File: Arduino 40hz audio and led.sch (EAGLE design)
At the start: 18 parts

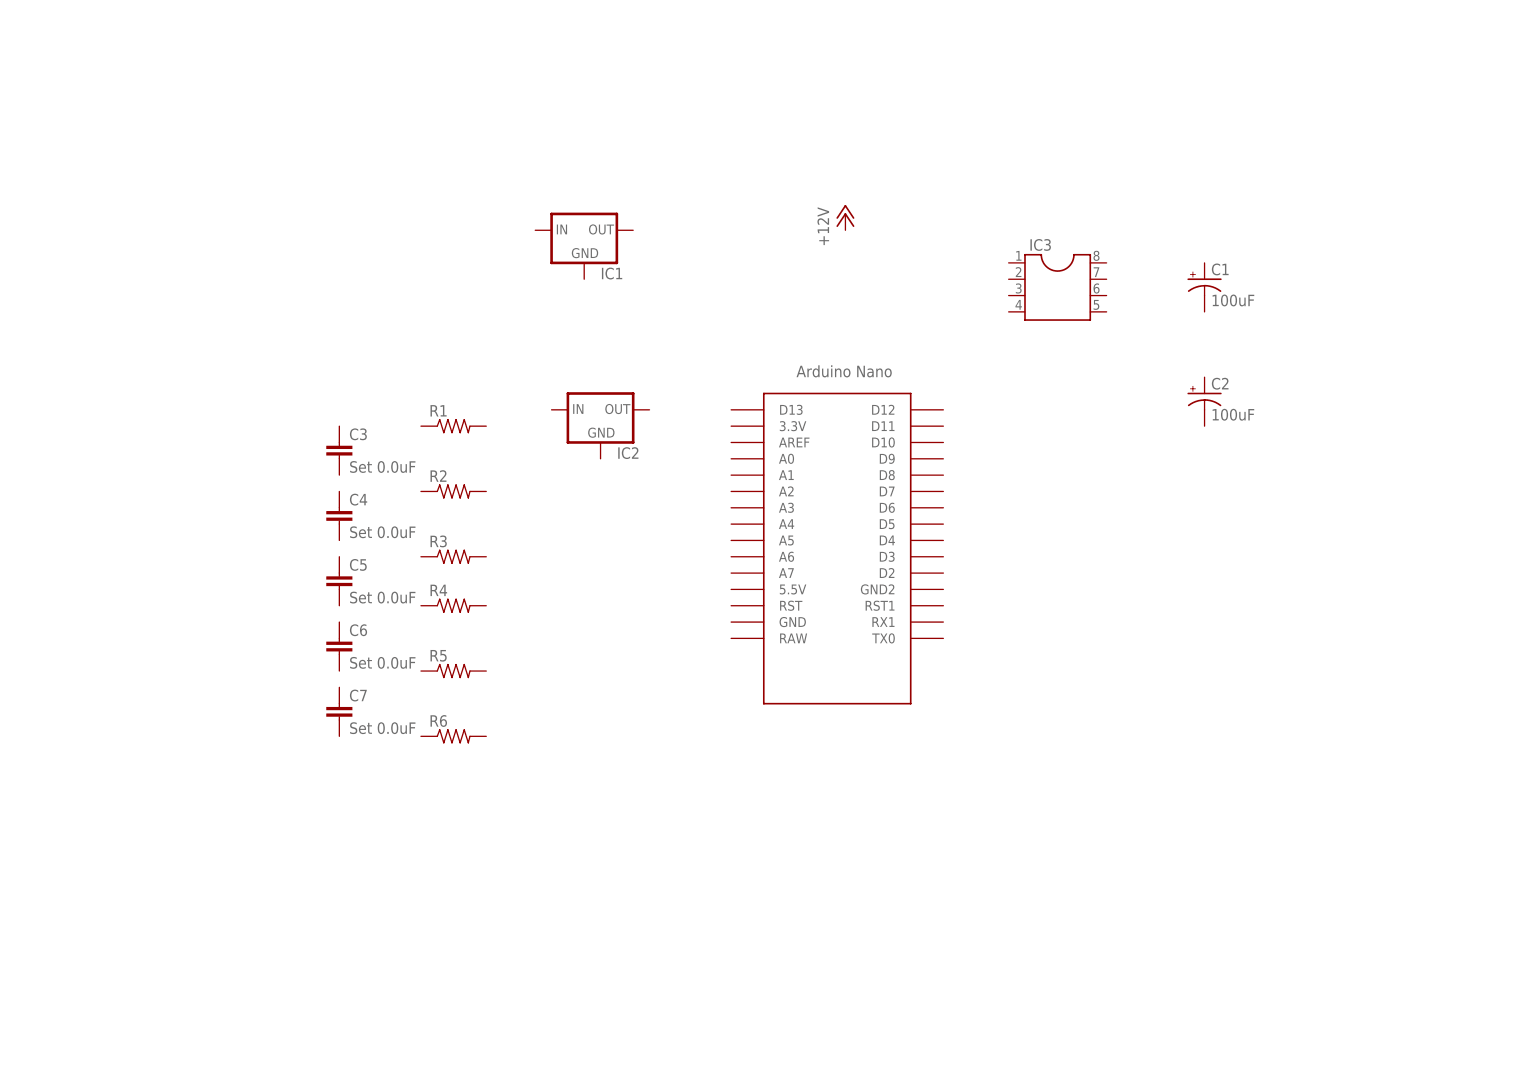
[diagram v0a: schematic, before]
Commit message: Initial schmatic and layout of board
Initial schmatic and layout of board

Still need to move some things around, add a couple of pads and change
some pad sizes.
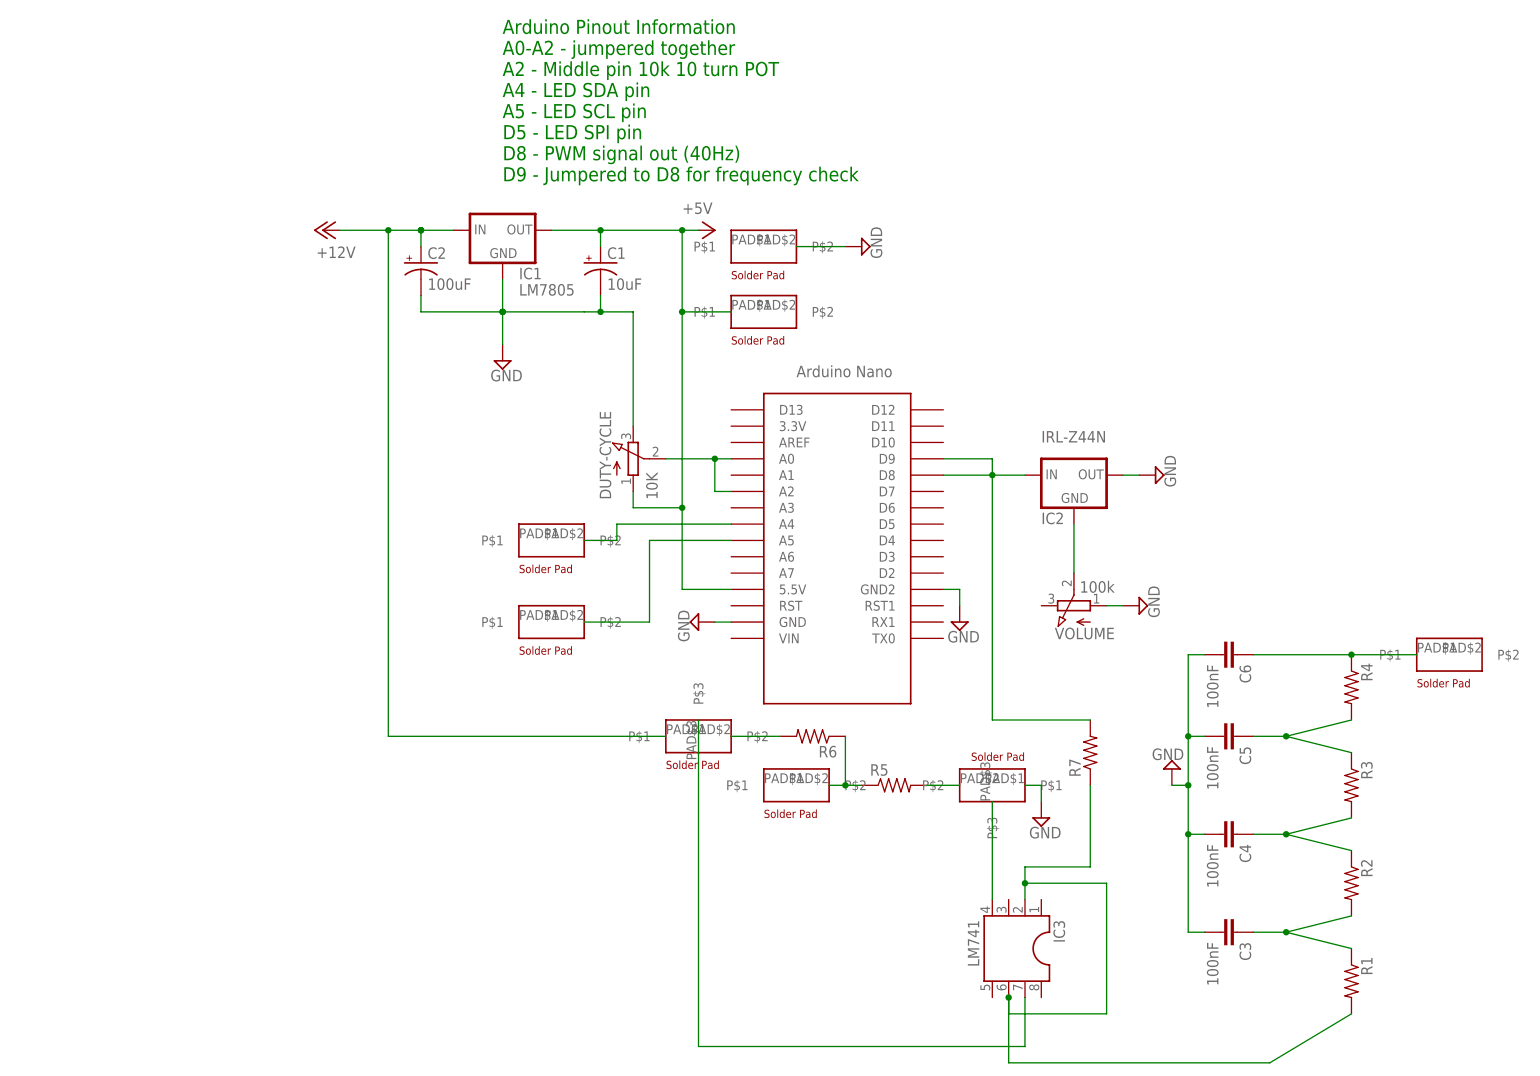
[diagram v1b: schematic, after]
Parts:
- removed C7: Set 0.0uF, jim_muppet_parts:CAP-MEDIUM-MUPPET
- added DUTY-CYCLE: 10K, jim_muppet_parts:POTENTIOMETER
- added LCD-GND: LCD-GND, jim_muppet_parts:PAD-2PIN-RECTANGLE
- added P+2: +5V, jim_muppet_parts:+5V
- added R7: (no value), jim_muppet_parts:RESISTORPTH-1/4W
- added U$2, U$4, U$6, U$7, U$8: PAD-2PIN-RECTANGLE, jim_muppet_parts:PAD-2PIN-RECTANGLE
- added U$3, U$5: PAD-3PIN-RECTANGLE50MIL, jim_muppet_parts:PAD-3PIN-RECTANGLE50MIL
- added VOLUME: 100k, jim_muppet_parts:POTENTIOMETER
- C1: value 100uF -> 10uF
- C3, C4, C5, C6: value Set 0.0uF -> 100nF
- IC1: value (none) -> LM7805
- IC2: value (none) -> IRL-Z44N
- IC3: value (none) -> LM741
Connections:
- new net +12V: C2.+, IC1.IN, P+1.+12V, U$5.P$1
- new net +5V: C1.+, DUTY-CYCLE.A, IC1.OUT, P+2.+5V, U$1.5.5V, U$7.P$1
- new net GND: C1.-, C2.-, C3.2, C4.2, C5.2, C6.2, DUTY-CYCLE.E, IC1.GND, IC2.OUT, LCD-GND.P$2, U$1.GND, U$1.GND2, U$3.P$1, VOLUME.A
- new net N$1: DUTY-CYCLE.S, U$1.A0, U$1.A2
- new net N$10: R5.2, U$3.P$2
- new net N$11: IC3.7, U$5.P$3
- new net N$12: IC3.4, U$3.P$3
- new net N$13: IC3.2, IC3.6, R1.2, R7.1
- new net N$14: U$1.A4, U$4.P$2
- new net N$15: U$1.A5, U$6.P$2
- new net N$2: IC2.IN, R7.2, U$1.D8, U$1.D9
- new net N$3: C3.1, R1.1, R2.2
- new net N$4: C4.1, R2.1, R3.2
- new net N$5: C5.1, R3.1, R4.2
- new net N$6: C6.1, R4.1, U$2.P$1
- new net N$7: R6.2, U$5.P$2
- new net N$8: IC2.GND, VOLUME.S
- new net N$9: R5.1, R6.1, U$8.P$2
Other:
- note added: "Arduino Pinout Information A0-A2 - jumpered together A2 - Middle pin 10k 10 turn POT A4 - LED SDA pin A5 - LED SCL pin D5 - LED SPI pin D8 - PWM signal out (40Hz) D9 - Jumpered to D8 for frequency check"
- moved on the sheet: C1, C2, C3, C4, C5, C6, IC1, IC2, IC3, R1, R2, R3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

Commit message: Updated schematic and board
Updated schematic and board. Made the board more compact.

Still need to fix a few issues with the board
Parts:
- removed LCD-GND: LCD-GND, jim_muppet_parts:PAD-2PIN-RECTANGLE
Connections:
- net GND: no longer LCD-GND.P$2
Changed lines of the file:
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@@
 <grid distance="0.1" unitdist="inch" unit="inch" style="lines" multiple="1" display="no" altdistance="0.01" altunitdist="inch" altunit="inch"/>
 <layers>
-<layer number="1" name="Top" color="4" fill="1" visible="yes" active="no"/>
-<layer number="2" name="Route2" color="16" fill="1" visible="yes" active="no"/>
-<layer number="3" name="Route3" color="17" fill="1" visible="yes" active="no"/>
-<layer number="4" name="Route4" color="18" fill="1" visible="yes" active="no"/>
-<layer number="5" name="Route5" color="19" fill="1" visible="yes" active="no"/>
-<layer number="6" name="Route6" color="25" fill="1" visible="yes" active="no"/>
-<layer number="7" name="Route7" color="26" fill="1" visible="yes" active="no"/>
-<layer number="8" name="Route8" color="27" fill="1" visible="yes" active="no"/>
-<layer number="9" name="Route9" color="28" fill="1" visible="yes" active="no"/>
-<layer number="10" name="Route10" color="29" fill="1" visible="yes" active="no"/>
-<layer number="11" name="Route11" color="30" fill="1" visible="yes" active="no"/>
-<layer number="12" name="Route12" color="20" fill="1" visible="yes" active="no"/>
-<layer number="13" name="Route13" color="21" fill="1" visible="yes" active="no"/>
-<layer number="14" name="Route14" color="22" fill="1" visible="yes" active="no"/>
-<layer number="15" name="Route15" color="23" fill="1" visible="yes" active="no"/>
-<layer number="16" name="Bottom" color="1" fill="1" visible="yes" active="no"/>
-<layer number="17" name="Pads" color="2" fill="1" visible="yes" active="no"/>
-<layer number="18" name="Vias" color="2" fill="1" visible="yes" active="no"/>
-<layer number="19" name="Unrouted" color="6" fill="1" visible="yes" active="no"/>
-<layer number="20" name="Dimension" color="24" fill="1" visible="yes" active="no"/>
-<layer number="21" name="tPlace" color="7" fill="1" visible="yes" active="no"/>
-<layer number="22" name="bPlace" color="7" fill="1" visible="yes" active="no"/>
-<layer number="23" name="tOrigins" color="15" fill="1" visible="yes" active="no"/>
-<layer number="24" name="bOrigins" color="15" fill="1" visible="yes" active="no"/>
-<layer number="25" name="tNames" color="7" fill="1" visible="yes" active="no"/>
-<layer number="26" name="bNames" color="7" fill="1" visible="yes" active="no"/>
-<layer number="27" name="tValues" color="7" fill="1" visible="yes" active="no"/>
-<layer number="28" name="bValues" color="7" fill="1" visible="yes" active="no"/>
+<layer number="1" name="Top" color="4" fill="1" visible="no" active="no"/>
+<layer number="2" name="Route2" color="16" fill="1" visible="no" active="no"/>
+<layer number="3" name="Route3" color="17" fill="1" visible="no" active="no"/>
+<layer number="4" name="Route4" color="18" fill="1" visible="no" active="no"/>
+<layer number="5" name="Route5" color="19" fill="1" visible="no" active="no"/>
+<layer number="6" name="Route6" color="25" fill="1" visible="no" active="no"/>
+<layer number="7" name="Route7" color="26" fill="1" visible="no" active="no"/>
+<layer number="8" name="Route8" color="27" fill="1" visible="no" active="no"/>
+<layer number="9" name="Route9" color="28" fill="1" visible="no" active="no"/>
+<layer number="10" name="Route10" color="29" fill="1" visible="no" active="no"/>
+<layer number="11" name="Route11" color="30" fill="1" visible="no" active="no"/>
+<layer number="12" name="Route12" color="20" fill="1" visible="no" active="no"/>
+<layer number="13" name="Route13" color="21" fill="1" visible="no" active="no"/>
+<layer number="14" name="Route14" color="22" fill="1" visible="no" active="no"/>
+<layer number="15" name="Route15" color="23" fill="1" visible="no" active="no"/>
+<layer number="16" name="Bottom" color="1" fill="1" visible="no" active="no"/>
+<layer number="17" name="Pads" color="2" fill="1" visible="no" active="no"/>
+<layer number="18" name="Vias" color="2" fill="1" visible="no" active="no"/>
+<layer number="19" name="Unrouted" color="6" fill="1" visible="no" active="no"/>
+<layer number="20" name="Dimension" color="24" fill="1" visible="no" active="no"/>
+<layer number="21" name="tPlace" color="7" fill="1" visible="no" active="no"/>
+<layer number="22" name="bPlace" color="7" fill="1" visible="no" active="no"/>
+<layer number="23" name="tOrigins" color="15" fill="1" visible="no" active="no"/>
+<layer number="24" name="bOrigins" color="15" fill="1" visible="no" active="no"/>
+<layer number="25" name="tNames" color="7" fill="1" visible="no" active="no"/>
+<layer number="26" name="bNames" color="7" fill="1" visible="no" active="no"/>
+<layer number="27" name="tValues" color="7" fill="1" visible="no" active="no"/>
+<layer number="28" name="bValues" color="7" fill="1" visible="no" active="no"/>
 <layer number="29" name="tStop" color="7" fill="3" visible="no" active="no"/>
 <layer number="30" name="bStop" color="7" fill="6" visible="no" active="no"/>
@@
 <layer number="35" name="tGlue" color="7" fill="4" visible="no" active="no"/>
 <layer number="36" name="bGlue" color="7" fill="5" visible="no" active="no"/>
-<layer number="37" name="tTest" color="7" fill="1" visible="yes" active="no"/>
-<layer number="38" name="bTest" color="7" fill="1" visible="yes" active="no"/>
+<layer number="37" name="tTest" color="7" fill="1" visible="no" active="no"/>
+<layer number="38" name="bTest" color="7" fill="1" visible="no" active="no"/>
 <layer number="39" name="tKeepout" color="4" fill="11" visible="no" active="no"/>
 <layer number="40" name="bKeepout" color="1" fill="11" visible="no" active="no"/>
@@
 <layer number="44" name="Drills" color="7" fill="1" visible="no" active="no"/>
 <layer number="45" name="Holes" color="7" fill="1" visible="no" active="no"/>
-<layer number="46" name="Milling" color="3" fill="1" visible="yes" active="no"/>
-<layer number="47" name="Measures" color="7" fill="1" visible="yes" active="no"/>
-<layer number="48" name="Document" color="7" fill="1" visible="yes" active="no"/>
-<layer number="49" name="Reference" color="7" fill="1" visible="yes" active="no"/>
-<layer number="50" name="dxf" color="7" fill="1" visible="yes" active="no"/>
-<layer number="51" name="tDocu" color="7" fill="1" visible="yes" active="no"/>
-<layer number="52" name="bDocu" color="7" fill="1" visible="yes" active="no"/>
-<layer number="53" name="tGND_GNDA" color="7" fill="9" visible="yes" active="no"/>
-<layer number="54" name="bGND_GNDA" color="1" fill="9" visible="yes" active="no"/>
-<layer number="56" name="wert" color="7" fill="1" visible="yes" active="no"/>
-<layer number="57" name="tCAD" color="7" fill="1" visible="yes" active="no"/>
-<layer number="59" name="tCarbon" color="7" fill="1" visible="yes" active="no"/>
-<layer number="60" name="bCarbon" color="7" fill="1" visible="yes" active="no"/>
+<layer number="46" name="Milling" color="3" fill="1" visible="no" active="no"/>
+<layer number="47" name="Measures" color="7" fill="1" visible="no" active="no"/>
+<layer number="48" name="Document" color="7" fill="1" visible="no" active="no"/>
+<layer number="49" name="Reference" color="7" fill="1" visible="no" active="no"/>
+<layer number="50" name="dxf" color="7" fill="1" visible="no" active="no"/>
+<layer number="51" name="tDocu" color="7" fill="1" visible="no" active="no"/>
+<layer number="52" name="bDocu" color="7" fill="1" visible="no" active="no"/>
+<layer number="53" name="tGND_GNDA" color="7" fill="9" visible="no" active="no"/>
+<layer number="54" name="bGND_GNDA" color="1" fill="9" visible="no" active="no"/>
+<layer number="56" name="wert" color="7" fill="1" visible="no" active="no"/>
+<layer number="57" name="tCAD" color="7" fill="1" visible="no" active="no"/>
+<layer number="59" name="tCarbon" color="7" fill="1" visible="no" active="no"/>
+<layer number="60" name="bCarbon" color="7" fill="1" visible="no" active="no"/>
 <layer number="88" name="SimResults" color="9" fill="1" visible="yes" active="yes"/>
 <layer number="89" name="SimProbes" color="9" fill="1" visible="yes" active="yes"/>
@@
 <part name="U$6" library="jim_muppet_parts" deviceset="PAD-2PIN-RECTANGLE" device=""/>
 <part name="U$7" library="jim_muppet_parts" deviceset="PAD-2PIN-RECTANGLE" device=""/>
-<part name="LCD-GND" library="jim_muppet_parts" deviceset="PAD-2PIN-RECTANGLE" device="" value="LCD-GND"/>
-<part name="SUPPLY8" library="supply2" library_urn="urn:adsk.eagle:library:372" deviceset="GND" device=""/>
 </parts>
 <sheets>
@@
 <instance part="U$6" gate="G$1" x="45.72" y="35.56" smashed="yes"/>
 <instance part="U$7" gate="G$1" x="78.74" y="83.82" smashed="yes"/>
-<instance part="LCD-GND" gate="G$1" x="78.74" y="93.98" smashed="yes"/>
-<instance part="SUPPLY8" gate="GND" x="93.98" y="93.98" smashed="yes" rot="R90">
-<attribute name="VALUE" x="97.155" y="92.075" size="1.778" layer="96" rot="R90"/>
-</instance>
 </instances>
 <busses>
@@
 <wire x1="121.92" y1="10.16" x2="121.92" y2="7.62" width="0.1524" layer="91"/>
 </segment>
-<segment>
-<pinref part="LCD-GND" gate="G$1" pin="P$2"/>
-<pinref part="SUPPLY8" gate="GND" pin="GND"/>
-<wire x1="83.82" y1="93.98" x2="91.44" y2="93.98" width="0.1524" layer="91"/>
-</segment>
 </net>

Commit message: Version 1 is done.. w00t
Version 1 is done.. w00t!!!

Now I need to make some little fixes as I've built the first one.
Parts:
- added JP1: (no value), jumper:JP1Q
- added JP2, JP3: (no value), jim_muppet_parts:JUMPER-JP1E
- added P+3: +6V, jim_muppet_parts:+6V
- added R8: (no value), jim_muppet_parts:RESISTORPTH-1/4W
- U$2: value PAD-2PIN-RECTANGLE -> -6v test point; device jim_muppet_parts:PAD-2PIN-RECTANGLE -> jim_muppet_parts:PROBE-POINTPROBE_POINT_1
- U$3: value PAD-3PIN-RECTANGLE50MIL -> SINE out; device jim_muppet_parts:PAD-3PIN-RECTANGLE50MIL -> jim_muppet_parts:PROBE-POINTPROBE_POINT_1
- U$5: value PAD-3PIN-RECTANGLE50MIL -> +/- 6v virt gnd; device jim_muppet_parts:PAD-3PIN-RECTANGLE50MIL -> jim_muppet_parts:PROBE-POINTPROBE_POINT_1
- U$8: value PAD-2PIN-RECTANGLE -> +6v test point; device jim_muppet_parts:PAD-2PIN-RECTANGLE -> jim_muppet_parts:PROBE-POINTPROBE_POINT_1
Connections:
- removed net N$11: IC3.7, U$5.P$3
- removed net N$12: IC3.4, U$3.P$3
- new net N$16: JP1.2, R5.1, U$5.P$1
- net +12V: now also IC3.7, JP2.1, R5.2, U$8.P$1; no longer U$5.P$1
- net +5V: now also IC2.GND, JP3.2, P+3.+5V; no longer U$1.5.5V
- net GND: now also IC3.4, R6.1, U$2.P$1; no longer U$3.P$1
- net N$10: now also IC3.2, R7.1, R8.2; no longer R5.2, U$3.P$2
- net N$13: now also R8.1; no longer IC3.2, R7.1
- net N$2: now also VOLUME.S
- net N$6: no longer U$2.P$1
- net N$7: now also JP1.1; no longer U$5.P$2
- net N$8: now also JP2.2, U$1.VIN; no longer IC2.GND, VOLUME.S
- net N$9: now also JP3.1, U$1.5.5V; no longer R5.1, R6.1, U$8.P$2
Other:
- moved on the sheet: C3, C4, C5, C6, IC3, R1, R2, R3, R4, R5, R6, R7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
